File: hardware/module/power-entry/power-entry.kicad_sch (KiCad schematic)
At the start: 32 parts

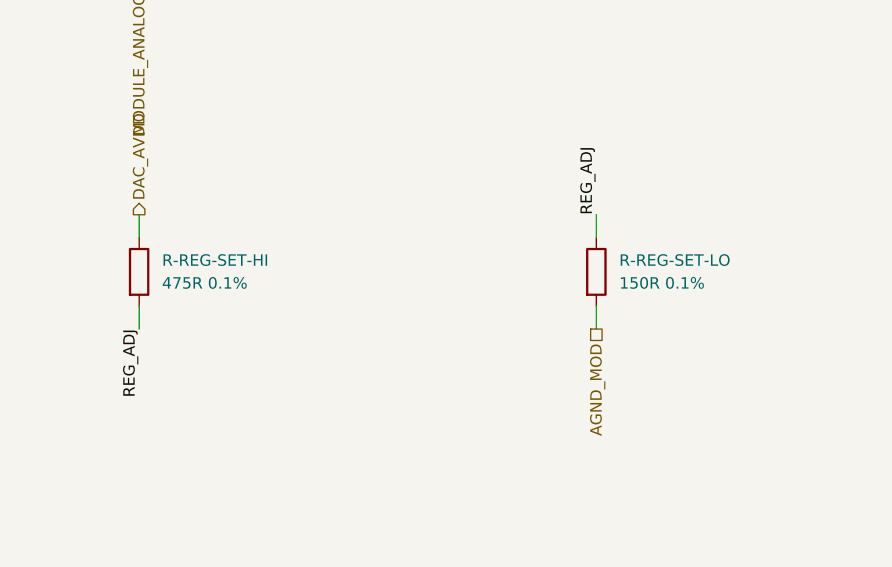
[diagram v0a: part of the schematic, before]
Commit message: U-LVL-MOD on DAC_AVDD (owner, option 1); LM317L divider values to their positions
The 74AHCT125 driving the DAC8568's SYNC/SCLK/DIN now takes its VCC (and
C-DEC-LVL) from DAC_AVDD, so its outputs can never sit over the DAC's
AVDD + 0.3 V absolute maximum while the two 5 V rails disagree.

R-REG-SET-HI (ADJ to OUT) and R-REG-SET-LO (ADJ to GND) carried each
other's values: as netlisted the LM317L set 1.25 x (1 + 150/475) = 1.65 V,
not dac-rail's 1.25 x (1 + 475/150). The sims had swapped the names back
silently. Values, MPN and LCSC swapped on the sheet and in the fragment.

Co-Authored-By: Claude Opus 5.5 <noreply@anthropic.com>
Claude-Session: https://claude.ai/code/session_01LmB4muFXnoLprWX4JzuJ5A
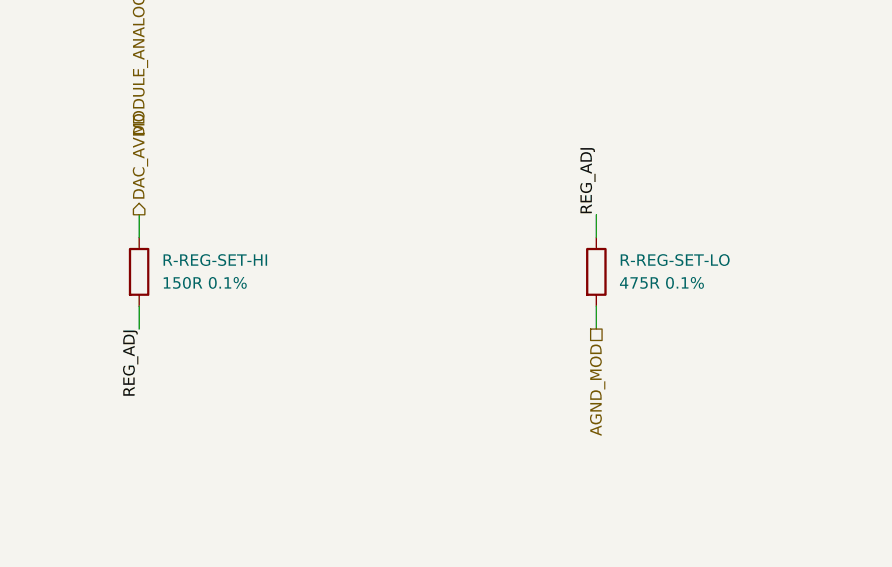
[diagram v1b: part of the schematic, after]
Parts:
- R-REG-SET-HI: value 475R 0.1% -> 150R 0.1%; LCSC C50670161 -> C513734; MPN TC0525B4750T5G -> RT0805BRD07150RL; Manufacturer UNI-ROYAL(Uniroyal Elec) -> YAGEO
- R-REG-SET-LO: value 150R 0.1% -> 475R 0.1%; LCSC C513734 -> C50670161; MPN RT0805BRD07150RL -> TC0525B4750T5G; Manufacturer YAGEO -> UNI-ROYAL(Uniroyal Elec)
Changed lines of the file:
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@@
     (in_bom yes) (on_board yes) (dnp no)
     (property "Reference" "R-REG-SET-HI" (at 297.18 186.69 0) (effects (font (size 1.27 1.27)) (justify left)))
-    (property "Value" "475R 0.1%" (at 297.18 189.23 0) (effects (font (size 1.27 1.27)) (justify left)))
+    (property "Value" "150R 0.1%" (at 297.18 189.23 0) (effects (font (size 1.27 1.27)) (justify left)))
     (property "Footprint" "Resistor_SMD:R_0805_2012Metric" (at 293.37 187.96 0) (effects (font (size 1.27 1.27)) hide))
     (property "Datasheet" "" (at 294.64 187.96 0) (effects (font (size 1.27 1.27)) hide))
     (property "Row" "R-REG-SET-HI" (at 294.64 187.96 0) (effects (font (size 1.27 1.27)) hide))
     (property "Pins" "1=1 2=2" (at 294.64 187.96 0) (effects (font (size 1.27 1.27)) hide))
-    (property "Manufacturer" "UNI-ROYAL(Uniroyal Elec)" (at 294.64 187.96 0) (effects (font (size 1.27 1.27)) hide))
-    (property "MPN" "TC0525B4750T5G" (at 294.64 187.96 0) (effects (font (size 1.27 1.27)) hide))
-    (property "LCSC" "C50670161" (at 294.64 187.96 0) (effects (font (size 1.27 1.27)) hide))
+    (property "Manufacturer" "YAGEO" (at 294.64 187.96 0) (effects (font (size 1.27 1.27)) hide))
+    (property "MPN" "RT0805BRD07150RL" (at 294.64 187.96 0) (effects (font (size 1.27 1.27)) hide))
+    (property "LCSC" "C513734" (at 294.64 187.96 0) (effects (font (size 1.27 1.27)) hide))
     (property "Assembly" "machine" (at 294.64 187.96 0) (effects (font (size 1.27 1.27)) hide))
     (pin "1")
@@
     (in_bom yes) (on_board yes) (dnp no)
     (property "Reference" "R-REG-SET-LO" (at 347.98 186.69 0) (effects (font (size 1.27 1.27)) (justify left)))
-    (property "Value" "150R 0.1%" (at 347.98 189.23 0) (effects (font (size 1.27 1.27)) (justify left)))
+    (property "Value" "475R 0.1%" (at 347.98 189.23 0) (effects (font (size 1.27 1.27)) (justify left)))
     (property "Footprint" "Resistor_SMD:R_0805_2012Metric" (at 344.17 187.96 0) (effects (font (size 1.27 1.27)) hide))
     (property "Datasheet" "" (at 345.44 187.96 0) (effects (font (size 1.27 1.27)) hide))
     (property "Row" "R-REG-SET-LO" (at 345.44 187.96 0) (effects (font (size 1.27 1.27)) hide))
     (property "Pins" "1=1 2=2" (at 345.44 187.96 0) (effects (font (size 1.27 1.27)) hide))
-    (property "Manufacturer" "YAGEO" (at 345.44 187.96 0) (effects (font (size 1.27 1.27)) hide))
-    (property "MPN" "RT0805BRD07150RL" (at 345.44 187.96 0) (effects (font (size 1.27 1.27)) hide))
-    (property "LCSC" "C513734" (at 345.44 187.96 0) (effects (font (size 1.27 1.27)) hide))
+    (property "Manufacturer" "UNI-ROYAL(Uniroyal Elec)" (at 345.44 187.96 0) (effects (font (size 1.27 1.27)) hide))
+    (property "MPN" "TC0525B4750T5G" (at 345.44 187.96 0) (effects (font (size 1.27 1.27)) hide))
+    (property "LCSC" "C50670161" (at 345.44 187.96 0) (effects (font (size 1.27 1.27)) hide))
     (property "Assembly" "machine" (at 345.44 187.96 0) (effects (font (size 1.27 1.27)) hide))
     (pin "1")

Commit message: Pre-layout fixes (F2): pitch sim deck to the netlist, mod jack range, ADR 0006 amendment, module power text
- pitch-stage/sim: one netlisted subcircuit (trim network, R-GAIN-CTR, follower
  at 1.02) placed with and without D-ESD-PITCH; DC transfer and trim ends added
- mod-jack-range and module-own-draw registered; mod-channels.md, power-entry.md,
  ADR 0006 corrected; power-off sim added to power-entry/sim
- stale sheet notes and BOM rows (U-REG-LOGIC, NT-AGND-MOD, FB2, R-ON-HI,
  C-BULK-RAIL, U-REG-DAC, J-PWR-EURO, U-ISO)

Sim results for pitch-stage, dac8568, mod-channels pending a run.

Co-Authored-By: Claude Opus 5.5 <noreply@anthropic.com>
Claude-Session: https://claude.ai/code/session_01LmB4muFXnoLprWX4JzuJ5A
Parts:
- FB2: Note THE UMBILICAL BRANCH. At its real operating current this be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 -> U-ISO's +12 V input leg; FB4 is its -12 V leg. They carry t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
- NT-AGND-MOD: Note The module analog star's single tie to PWR_GND, at the powe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 -> The module analog star's single tie: AGND_MOD to BUS_GND, a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
- U-REG-LOGIC: Note The module's own 5 V, for U-LVL-MOD: the bus +5 V is not us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 -> The module's own 5 V, LOGIC_5V: the SPI receiver U-RX-MOD a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
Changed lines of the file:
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@@
     (property "Pins" "1=1 2=2" (at 243.84 142.24 0) (effects (font (size 1.27 1.27)) hide))
     (property "Drawn_as" "FB2" (at 243.84 142.24 0) (effects (font (size 1.27 1.27)) hide))
-    (property "Note" "THE UMBILICAL BRANCH. At its real operating current this bead gives roughly half its nameplate impedance - see the FB-IN row, which is the only one of the four where that matters" (at 243.84 142.24 0) (effects (font (size 1.27 1.27)) hide))
+    (property "Note" "U-ISO's +12 V input leg; FB4 is its -12 V leg. They carry the converter's input, ~0.22 A in typical play, which puts them between the bias curve's 0 and 250 mA traces (ferrite-bias-impedance): the two of the four where DC bias matters - see the FB-IN row" (at 243.84 142.24 0) (effects (font (size 1.27 1.27)) hide))
     (property "Manufacturer" "Laird" (at 243.84 142.24 0) (effects (font (size 1.27 1.27)) hide))
     (property "MPN" "MI1206K601R-10" (at 243.84 142.24 0) (effects (font (size 1.27 1.27)) hide))
@@
     (property "Row" "NT-AGND-MOD" (at 193.04 233.68 0) (effects (font (size 1.27 1.27)) hide))
     (property "Pins" "1=1 2=2" (at 193.04 233.68 0) (effects (font (size 1.27 1.27)) hide))
-    (property "Note" "The module analog star's single tie to PWR_GND, at the power header's ground pins (power-entry.md, Grounding): copper only" (at 193.04 233.68 0) (effects (font (size 1.27 1.27)) hide))
+    (property "Note" "The module analog star's single tie: AGND_MOD to BUS_GND, at the power header's ground pins (power-entry.md, Grounding): copper only. PWR_GND reaches the star only through NT-UMB-MOD and NT-DIG-MOD" (at 193.04 233.68 0) (effects (font (size 1.27 1.27)) hide))
     (property "Pins_source" "a net tie's two pads: 1 the analog star (AGND_MOD), 2 PWR_GND at the header's ground pins" (at 193.04 233.68 0) (effects (font (size 1.27 1.27)) hide))
     (property "Manufacturer" "" (at 193.04 233.68 0) (effects (font (size 1.27 1.27)) hide))
@@
     (property "Pins" "VIN=1(VIN) GND=2(GND) EN=3(EN) SENSE=4(SENSE/ADJ) VOUT=5(VOUT)" (at 91.44 279.4 0) (effects (font (size 1.27 1.27)) hide))
     (property "Pins_source" "datasheets/discrete-and-power/ADI-ADP7118.pdf p.6 Figure 4 (5-lead TSOT): 1 VIN, 2 GND, 3 EN, 4 SENSE/ADJ, 5 VOUT. The symbol is KiCad's ADP7142AUJZ, whose TSOT-5 pinout is the same" (at 91.44 279.4 0) (effects (font (size 1.27 1.27)) hide))
-    (property "Note" "The module's own 5 V, for U-LVL-MOD: the bus +5 V is not used (owner, 2026-09-30). From the protected analog +12 V; EN tied to VIN; SENSE to VOUT at the part. GND on DIG_GND, the logic's return" (at 91.44 279.4 0) (effects (font (size 1.27 1.27)) hide))
+    (property "Note" "The module's own 5 V, LOGIC_5V: the SPI receiver U-RX-MOD and CS_MOD's pull-up (U-LVL-MOD is on DAC_AVDD); the bus +5 V is not used (owner, 2026-09-30). From the protected analog +12 V; EN tied to VIN; SENSE to VOUT at the part. GND on DIG_GND, the logic's return" (at 91.44 279.4 0) (effects (font (size 1.27 1.27)) hide))
     (property "Manufacturer" "Analog Devices" (at 91.44 279.4 0) (effects (font (size 1.27 1.27)) hide))
     (property "MPN" "ADP7118AUJZ-5.0-R7" (at 91.44 279.4 0) (effects (font (size 1.27 1.27)) hide))

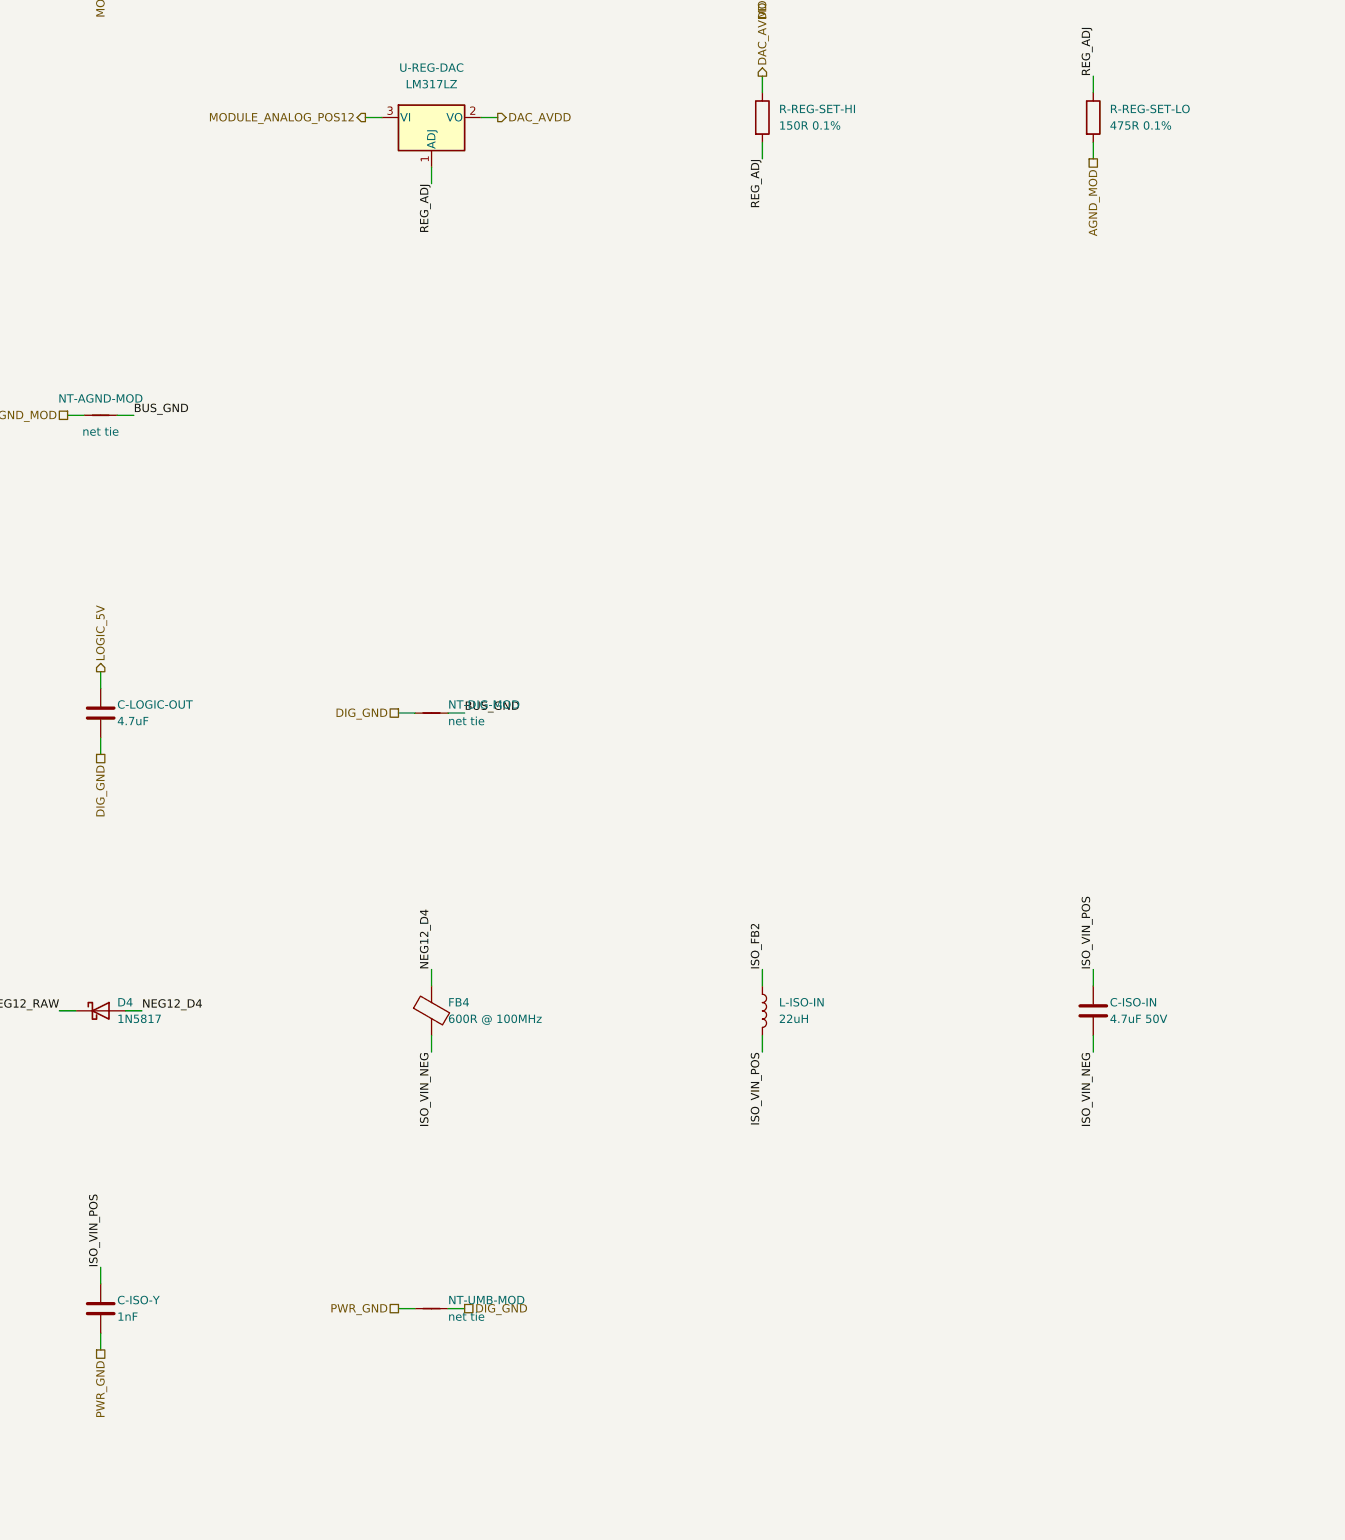
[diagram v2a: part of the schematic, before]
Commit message: WIP module power-entry: L-CM-ISO common-mode choke, C-ISO-Y 22 nF, TRIM-DAC-RAIL, dac-rail 5.20 V (A4-1, A8-8, A8-3)
Sheet, export, BOM rows, new sims (cm-loop, iso-input-z, dac-trim-*), datasheets
banked (manifest row follows). Pages and dependants follow in the next commits.

Co-Authored-By: Claude Opus 5.5 <noreply@anthropic.com>
Claude-Session: https://claude.ai/code/session_01LmB4muFXnoLprWX4JzuJ5A
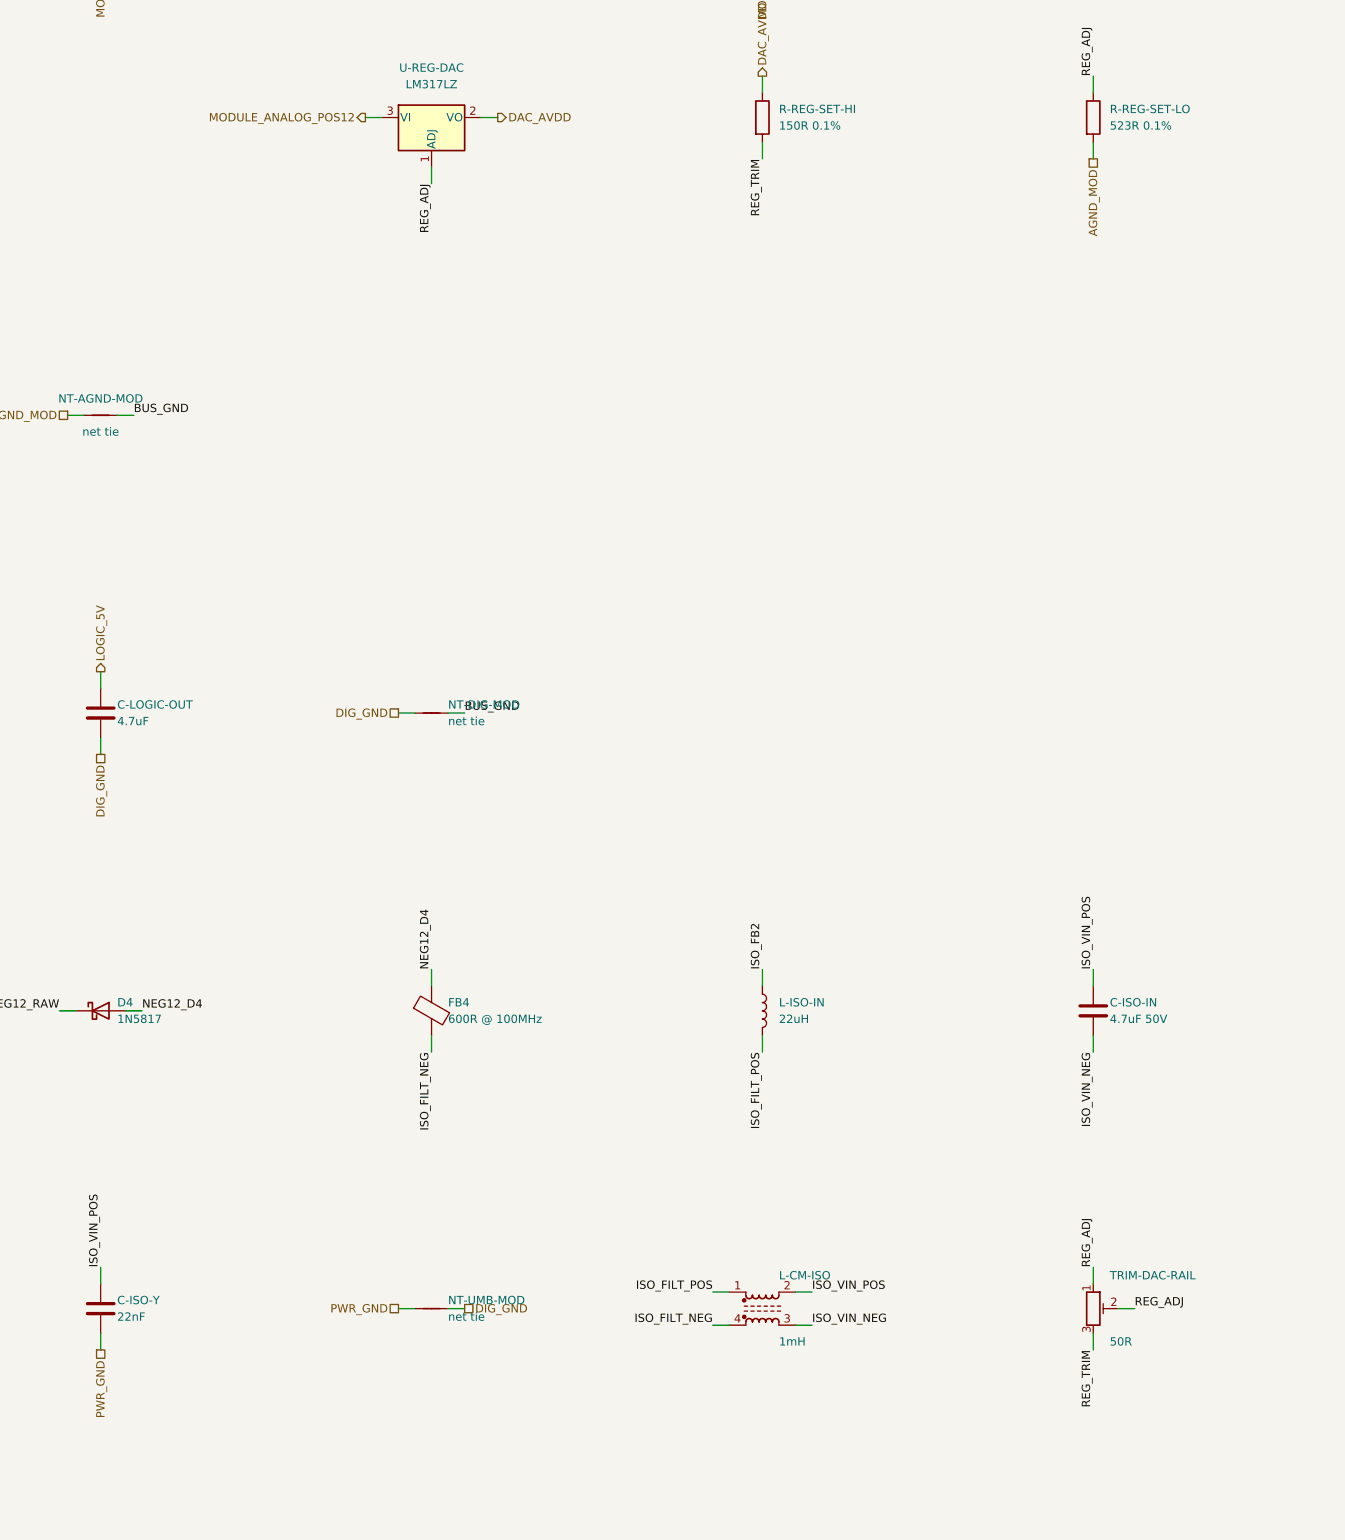
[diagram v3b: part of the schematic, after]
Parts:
- added L-CM-ISO: 1mH, woody:L_CommonModeChoke_Bourns_PM3700, symbol Filter:Choke_CommonMode_FerriteCore_1243
- added TRIM-DAC-RAIL: 50R, Potentiometer_SMD:Potentiometer_Bourns_3224W_Vertical, symbol Device:R_Potentiometer_Trim
- C-ISO-Y: value 1nF -> 22nF; LCSC C62774 -> C77069; MPN CC0805JRNPO9BN102 -> GRM21B5C1H223JA01L; Manufacturer YAGEO -> Murata; Note Across the isolation barrier AT the converter, ISO_VIN_POS to PWR_GND: gives the switching common-mode current a 1 nF path home beside U-ISO instead of round the star and the ribbon (RECOM's RPA20 filter has no Y-capacitor, PD-7; one 1 nF here against its 1100pF isolation capacitance, PD-5). On the +12 V side so PTC-ISO covers it if it fails short -> Across the isolation barrier AT the converter, ISO_VIN_POS to PWR_GND: with L-CM-ISO in the loop it takes the 550 kHz current through U-ISO's isolation capacitance (1100 pF typ, RECOM-RPA20-AW.pdf PD-5) home beside the converter. 22 nF C0G 50 V, chosen with the choke by power-entry/sim 'cm-loop' (power-entry.md, The common mode). On the +12 V side so PTC-ISO covers it if it fails short
- FB1, FB3: Note (none) -> ORDERED AS MI1206K601R-10: JLC sources it through Global So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
- FB2: Note U-ISO's +12 V input leg; FB4 is its -12 V leg. They carry the converter's input, ~0.22 A in typical play, which puts them between the bias curve's 0 and 250 mA traces (ferrite-bias-impedance): the two of the four where DC bias matters - see the FB-IN row -> U-ISO's +12 V input leg; FB4 is its -12 V leg. They carry the converter's input, ~0.22 A in typical play, which puts them between the bias curve's 0 and 250 mA traces (ferrite-bias-impedance): the two of the four where DC bias matters - see the FB-IN row. ORDERED AS MI1206K601R-10: JLC sources it through Global Sourcing / consignment (owner, 2026-10-01), so it stays machine-placed though LCSC lists 0 - see the FB-IN row
- FB4: Note The converter branch's -12 V leg, the partner of FB2 -> The converter branch's -12 V leg, the partner of FB2. ORDER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
- R-REG-SET-LO: value 475R 0.1% -> 523R 0.1%; LCSC C50670161 -> C47116002; MPN TC0525B4750T5G -> PTFR0805B523RN9; Manufacturer UNI-ROYAL(Uniroyal Elec) -> RESI
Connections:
- net ISO_VIN_NEG: now also L-CM-ISO.3; no longer FB4.2
- net ISO_VIN_POS: now also L-CM-ISO.2; no longer L-ISO-IN.2
- net REG_ADJ: now also TRIM-DAC-RAIL.1, TRIM-DAC-RAIL.2; no longer R-REG-SET-HI.2
- new net ISO_FILT_NEG: FB4.2, L-CM-ISO.4
- new net ISO_FILT_POS: L-CM-ISO.1, L-ISO-IN.2
- new net REG_TRIM: R-REG-SET-HI.2, TRIM-DAC-RAIL.3
